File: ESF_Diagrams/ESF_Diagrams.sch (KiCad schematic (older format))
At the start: 91 parts, among them M1 Motor, M2 Motor, U2 AIR, U3 AIR

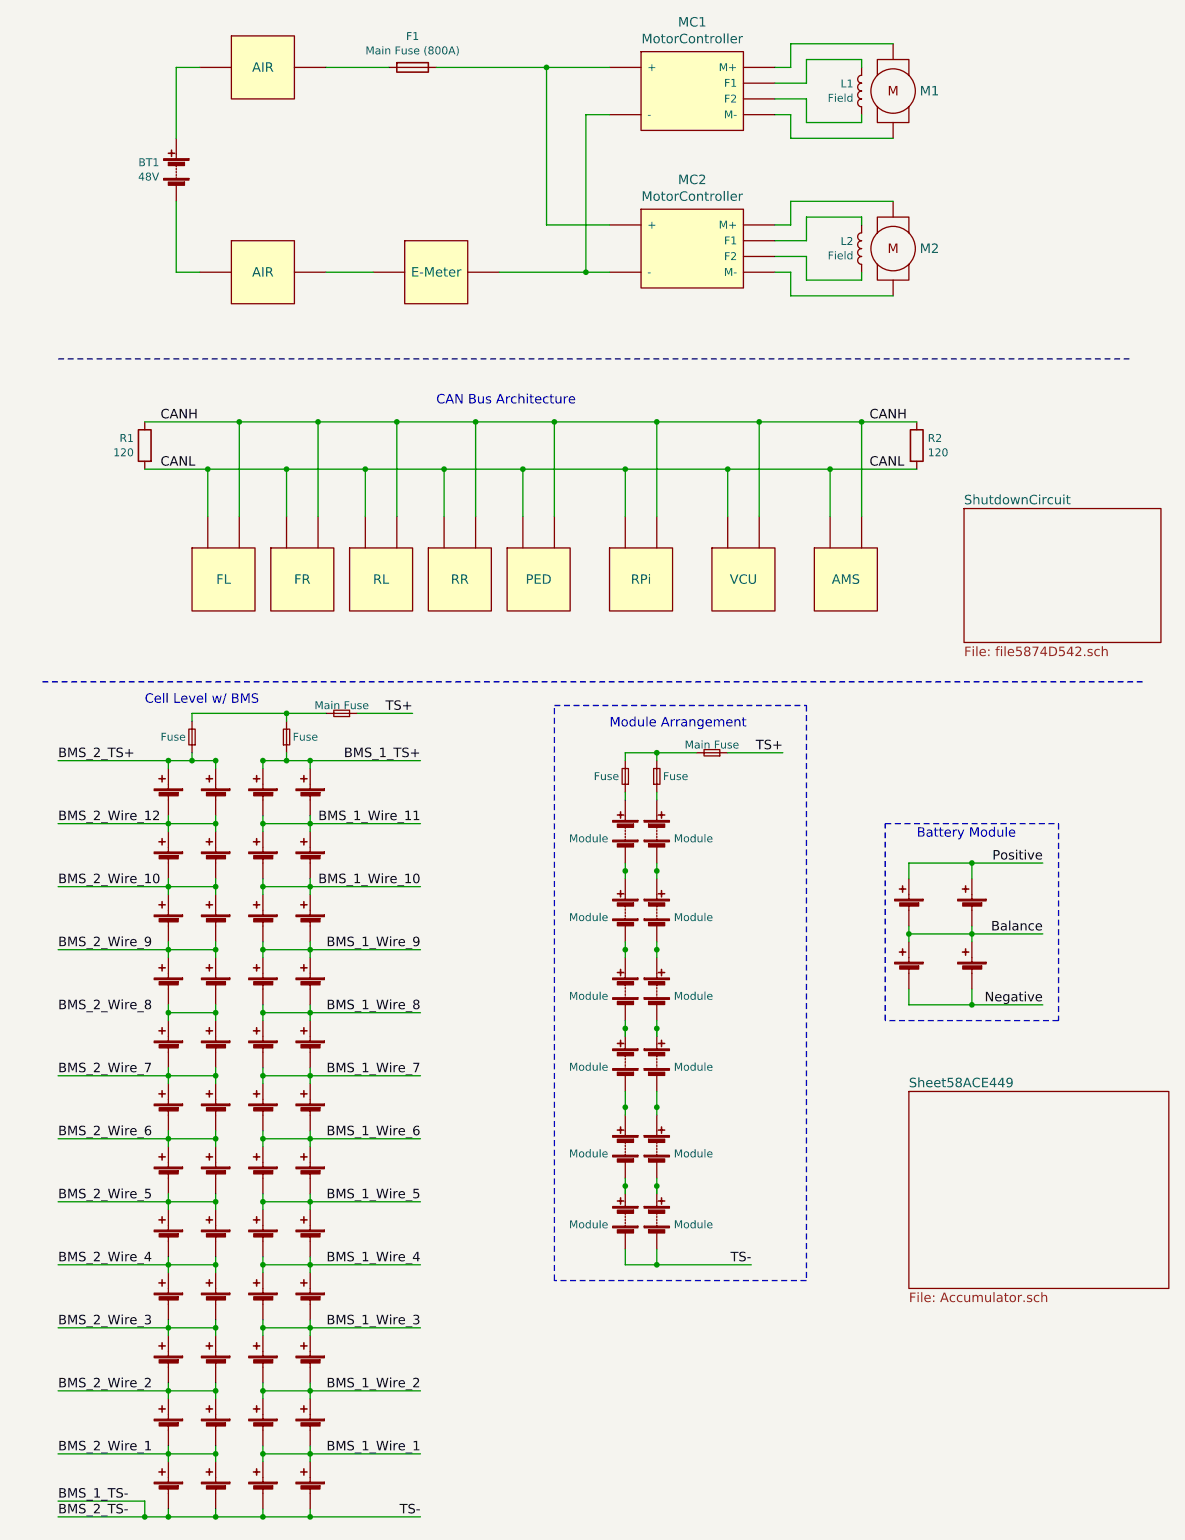
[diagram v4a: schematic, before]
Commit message: Add boxes to ESF Diagram
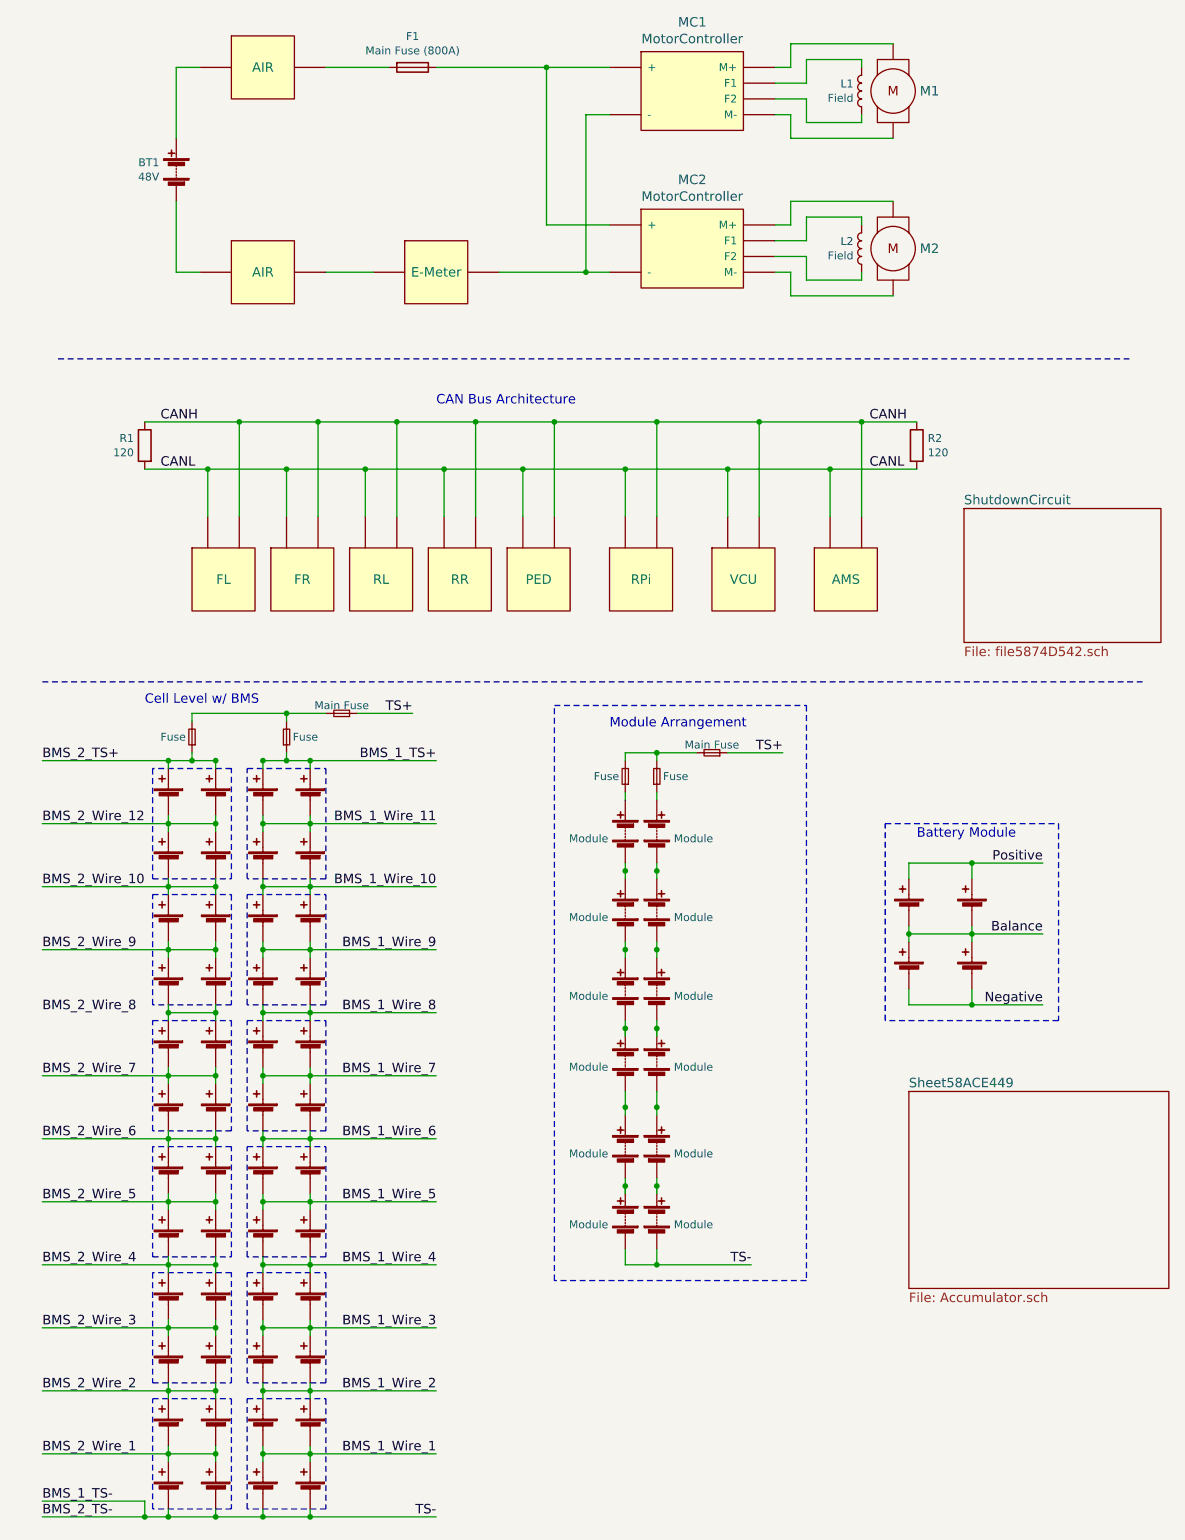
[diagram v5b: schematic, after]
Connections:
- net at MC1.~ (M-): now also L1.2; no longer M1.~
- net at MC2.~ (M-): now also L2.2; no longer M2.~
- new net: F1.1, MC1.~ (M-), MC2.~ (M-)
- new net: MC1.~ (M-), MC2.~ (M-), U?.~
- new net: M1.~, MC1.~ (M-)
- new net: M2.~, MC2.~ (M-)

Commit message: ESF Fixes
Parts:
- removed BT? (x52): Battery_Cell, symbol Battery_Cell
- removed BT? (x12): Module, symbol Battery
- removed F? (x4): Fuse, symbol Fuse_Small
- removed F? (x2): Main Fuse, symbol Fuse_Small
- added J?: Accumulator_OUT, symbol CONN_01X02
- added J?: MC_Left, symbol CONN_01X02
- added J?: MC_Right, symbol CONN_01X02
- added J?: HVD/E-Meter IN, symbol CONN_01X02
- added J?: HVD/E-Meter OUT, symbol CONN_01X02
- added J?: Accumulator IN, symbol CONN_01X02
- gave numbers to parts that had none: 9
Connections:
- net at MC1.~ (M-): now also L1.2; no longer M1.~
- net at MC2.~ (M-): now also L2.2; no longer M2.~
- new net: F1.1, MC1.~ (M-), MC2.~ (M-)
- new net: MC1.~ (M-), MC2.~ (M-), U6.~
- new net: M1.~, MC1.~ (M-)
- new net: M2.~, MC2.~ (M-)
- new net: J?.1 (P1), J?.2 (P2) (x5)
- new net TSMS: J?.1 (P1)
- new net To_AIR: J?.2 (P2)
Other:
- note removed: "Battery Module"
- note removed: "Cell Level w/ BMS"
- note removed: "Module Arrangement"

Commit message: Build the Shutdown Circuit in the ESF Diagram
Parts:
- gave numbers to parts that had none: 6
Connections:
- net at MC1.~ (M-): now also L1.2; no longer M1.~
- net at MC2.~ (M-): now also L2.2; no longer M2.~
- new net: F1.1, MC1.~ (M-), MC2.~ (M-)
- new net: MC1.~ (M-), MC2.~ (M-), U6.~
- new net: M1.~, MC1.~ (M-)
- new net: M2.~, MC2.~ (M-)
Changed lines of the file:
@@
 $EndSheet
 $Comp
-L CONN_01X02 J?
+L CONN_01X02 J1
 U 1 1 58CD8423
 P 5050 6500
-F 0 "J?" H 5050 6650 50  0001 C CNN
+F 0 "J1" H 5050 6650 50  0001 C CNN
 F 1 "Accumulator_OUT" H 5450 6550 50  0000 C CNN
 F 2 "" H 5050 6500 50  0001 C CNN
@@
 TSMS
 $Comp
-L CONN_01X02 J?
+L CONN_01X02 J2
 U 1 1 58CD8CAA
 P 5050 6850
-F 0 "J?" H 5050 7000 50  0001 C CNN
+F 0 "J2" H 5050 7000 50  0001 C CNN
 F 1 "MC_Left" H 5250 6850 50  0000 C CNN
 F 2 "" H 5050 6850 50  0001 C CNN
@@
 	4750 6800 4850 6800
 $Comp
-L CONN_01X02 J?
+L CONN_01X02 J3
 U 1 1 58CD8DFF
 P 5050 7200
-F 0 "J?" H 5050 7350 50  0001 C CNN
+F 0 "J3" H 5050 7350 50  0001 C CNN
 F 1 "MC_Right" H 5300 7200 50  0000 C CNN
 F 2 "" H 5050 7200 50  0001 C CNN
@@
 	4750 7150 4850 7150
 $Comp
-L CONN_01X02 J?
+L CONN_01X02 J4
 U 1 1 58CD90D8
 P 5050 7550
-F 0 "J?" H 5050 7700 50  0001 C CNN
+F 0 "J4" H 5050 7700 50  0001 C CNN
 F 1 "HVD/E-Meter IN" H 5450 7600 50  0000 C CNN
 F 2 "" H 5050 7550 50  0001 C CNN
@@
 	4750 7500 4850 7500
 $Comp
-L CONN_01X02 J?
+L CONN_01X02 J5
 U 1 1 58CDA10A
 P 5050 7900
-F 0 "J?" H 5050 8050 50  0001 C CNN
+F 0 "J5" H 5050 8050 50  0001 C CNN
 F 1 "HVD/E-Meter OUT" H 5450 7950 50  0000 C CNN
 F 2 "" H 5050 7900 50  0001 C CNN
@@
 	4750 7850 4850 7850
 $Comp
-L CONN_01X02 J?
+L CONN_01X02 J6
 U 1 1 58CDA574
 P 5050 8250
-F 0 "J?" H 5050 8400 50  0001 C CNN
+F 0 "J6" H 5050 8400 50  0001 C CNN
 F 1 "Accumulator IN" H 5450 8300 50  0000 C CNN
 F 2 "" H 5050 8250 50  0001 C CNN

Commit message: Fix error in Precharge Circuit in ESF Diagram
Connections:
- net at MC1.~ (M-): now also L1.2; no longer M1.~
- net at MC2.~ (M-): now also L2.2; no longer M2.~
- new net: F1.1, MC1.~ (M-), MC2.~ (M-)
- new net: MC1.~ (M-), MC2.~ (M-), U6.~
- new net: M1.~, MC1.~ (M-)
- new net: M2.~, MC2.~ (M-)
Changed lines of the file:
@@
 	1600 1250 1750 1250
 Wire Wire Line
-	3250 1250 3950 1250
-Wire Wire Line
-	3950 1250 4350 1250
+	3250 1250 4350 1250
 Wire Wire Line
 	4350 2250 3950 2250
@@
 	5950 2600 5950 2550
 Wire Wire Line
-	1400 3500 2000 3500
-Wire Wire Line
-	2000 3500 2500 3500
-Wire Wire Line
-	2500 3500 3000 3500
-Wire Wire Line
-	3000 3500 3500 3500
-Wire Wire Line
-	3500 3500 4000 3500
-Wire Wire Line
-	4000 3500 4650 3500
-Wire Wire Line
-	4650 3500 5300 3500
-Wire Wire Line
-	5300 3500 5950 3500
-Wire Wire Line
-	5950 3500 6300 3500
+	1400 3500 6300 3500
 Wire Wire Line
 	2000 3500 2000 4100
@@
 Connection ~ 5750 3800
 Wire Wire Line
-	1400 3800 1800 3800
-Wire Wire Line
-	1800 3800 2300 3800
-Wire Wire Line
-	2300 3800 2800 3800
-Wire Wire Line
-	2800 3800 3300 3800
-Wire Wire Line
-	3300 3800 3800 3800
-Wire Wire Line
-	3800 3800 4450 3800
-Wire Wire Line
-	4450 3800 5100 3800
-Wire Wire Line
-	5100 3800 5750 3800
-Wire Wire Line
-	5750 3800 6300 3800
+	1400 3800 6300 3800
 Wire Notes Line
 	850  3100 7650 3100
@@
 	2850 2550 2550 2550
 Wire Wire Line
-	3650 2550 4200 2550
-Wire Wire Line
-	4200 2550 4350 2550
+	3650 2550 4350 2550
 $Sheet
 S 750  5400 1650 1250
